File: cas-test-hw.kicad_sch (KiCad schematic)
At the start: 3 parts

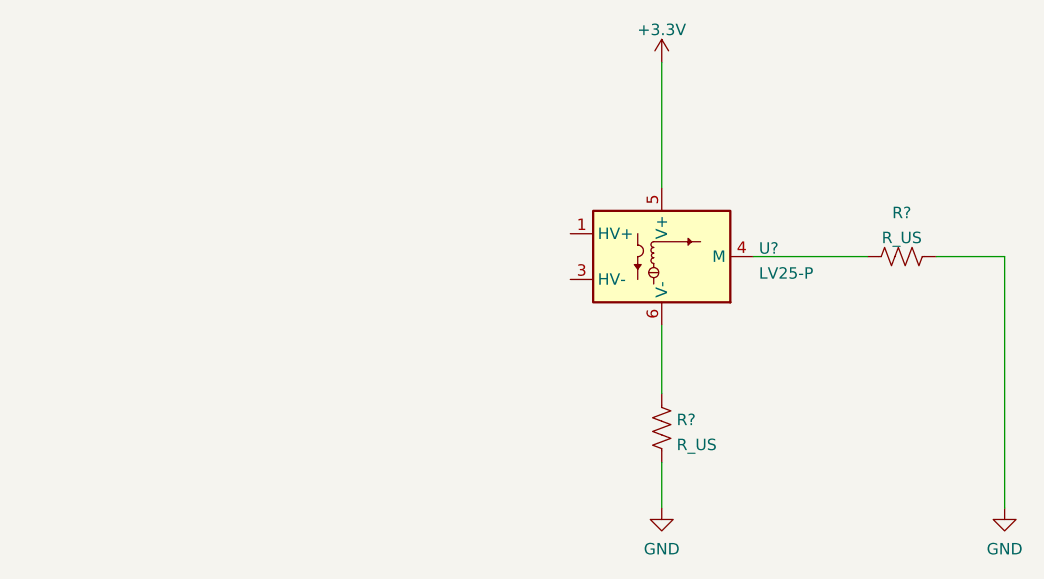
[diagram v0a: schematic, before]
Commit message: added mosfet
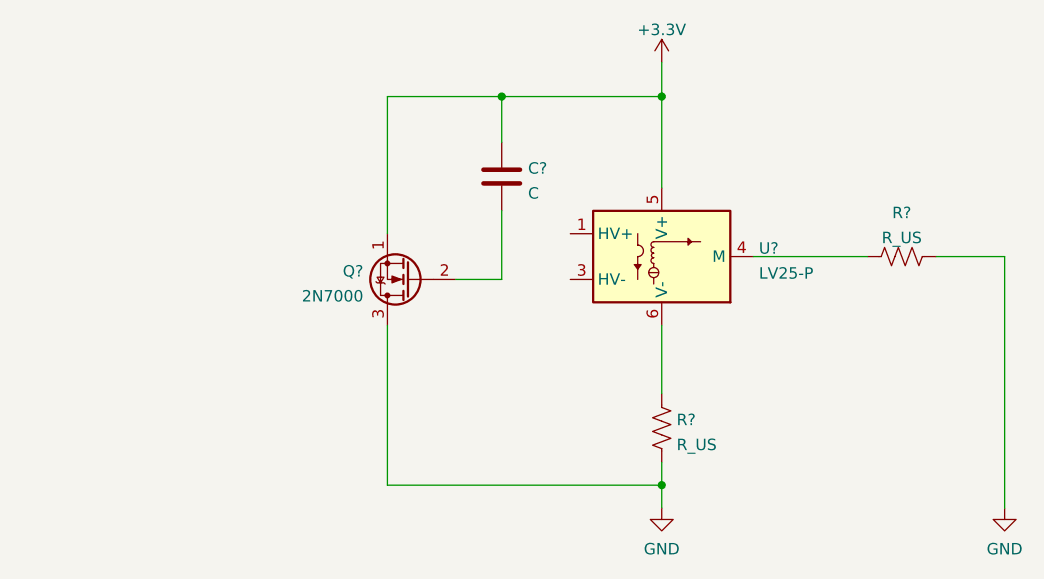
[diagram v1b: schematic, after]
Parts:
- added C?: C, symbol Device:C
- added Q?: 2N7000, Package_TO_SOT_THT:TO-92_Inline, symbol Transistor_FET:2N7000
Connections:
- net +3V3: now also C?.1, Q?.1 (S)
- net GND: now also Q?.3 (D)
- new net: C?.2, Q?.2 (G)
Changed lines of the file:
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@@
 (kicad_sch (version 20210621) (generator eeschema)
   (paper "A4")
-  (wire (pts (xy 123.19 78.74) (xy 123.19 92.71))
+  (junction (at 105.41 82.55) (diameter 0) (color 0 0 0 0))
+  (junction (at 123.19 82.55) (diameter 0) (color 0 0 0 0))
+  (junction (at 123.19 125.73) (diameter 0) (color 0 0 0 0))
+  (wire (pts (xy 92.71 82.55) (xy 105.41 82.55))
+    (stroke (width 0) (type default) (color 0 0 0 0))
+  )
+  (wire (pts (xy 92.71 97.79) (xy 92.71 82.55))
+    (stroke (width 0) (type default) (color 0 0 0 0))
+  )
+  (wire (pts (xy 92.71 107.95) (xy 92.71 125.73))
+    (stroke (width 0) (type default) (color 0 0 0 0))
+  )
+  (wire (pts (xy 92.71 125.73) (xy 123.19 125.73))
+    (stroke (width 0) (type default) (color 0 0 0 0))
+  )
+  (wire (pts (xy 100.33 102.87) (xy 105.41 102.87))
+    (stroke (width 0) (type default) (color 0 0 0 0))
+  )
+  (wire (pts (xy 105.41 82.55) (xy 105.41 87.63))
+    (stroke (width 0) (type default) (color 0 0 0 0))
+  )
+  (wire (pts (xy 105.41 82.55) (xy 123.19 82.55))
+    (stroke (width 0) (type default) (color 0 0 0 0))
+  )
+  (wire (pts (xy 105.41 95.25) (xy 105.41 102.87))
+    (stroke (width 0) (type default) (color 0 0 0 0))
+  )
+  (wire (pts (xy 123.19 78.74) (xy 123.19 82.55))
+    (stroke (width 0) (type default) (color 0 0 0 0))
+  )
+  (wire (pts (xy 123.19 82.55) (xy 123.19 92.71))
     (stroke (width 0) (type default) (color 0 0 0 0))
   )
@@
     (stroke (width 0) (type default) (color 0 0 0 0))
   )
-  (wire (pts (xy 123.19 123.19) (xy 123.19 128.27))
+  (wire (pts (xy 123.19 123.19) (xy 123.19 125.73))
+    (stroke (width 0) (type default) (color 0 0 0 0))
+  )
+  (wire (pts (xy 123.19 125.73) (xy 123.19 128.27))
     (stroke (width 0) (type default) (color 0 0 0 0))
   )
@@
     (pin "1")
     (pin "2")
+  )
+  (symbol (lib_id "Device:C") (at 105.41 91.44 0) (unit 1)
+    (in_bom yes) (on_board yes) (fields_autoplaced)
+    (property "Reference" "C?" (id 0) (at 108.331 90.5315 0)
+      (effects (font (size 1.27 1.27)) (justify left))
+    )
+    (property "Value" "C" (id 1) (at 108.331 93.3066 0)
+      (effects (font (size 1.27 1.27)) (justify left))
+    )
+    (property "Footprint" "" (id 2) (at 106.3752 95.25 0)
+      (effects (font (size 1.27 1.27)) hide)
+    )
+    (property "Datasheet" "~" (id 3) (at 105.41 91.44 0)
+      (effects (font (size 1.27 1.27)) hide)
+    )
+    (pin "1")
+    (pin "2")
+  )
+  (symbol (lib_id "Transistor_FET:2N7000") (at 95.25 102.87 180) (unit 1)
+    (in_bom yes) (on_board yes) (fields_autoplaced)
+    (property "Reference" "Q?" (id 0) (at 90.043 101.9615 0)
+      (effects (font (size 1.27 1.27)) (justify left))
+    )
+    (property "Value" "2N7000" (id 1) (at 90.043 104.7366 0)
+      (effects (font (size 1.27 1.27)) (justify left))
+    )
+    (property "Footprint" "Package_TO_SOT_THT:TO-92_Inline" (id 2) (at 90.17 100.965 0)
+      (effects (font (size 1.27 1.27) italic) (justify left) hide)
+    )
+    (property "Datasheet" "https://www.onsemi.com/pub/Collateral/NDS7002A-D.PDF" (id 3) (at 95.25 102.87 0)
+      (effects (font (size 1.27 1.27)) (justify left) hide)
+    )
+    (pin "1")
+    (pin "2")
+    (pin "3")
   )
   (symbol (lib_id "Sensor_Voltage:LV25-P") (at 123.19 100.33 0) (unit 1)
@@
       (reference "#PWR?") (unit 1) (value "GND") (footprint "")
     )
+    (path "/f3cbb385-5d5b-4802-a5c7-511f3f3faef6"
+      (reference "C?") (unit 1) (value "C") (footprint "")
+    )
+    (path "/31f72fb0-d275-4aa4-b7ef-002a0a293743"
+      (reference "Q?") (unit 1) (value "2N7000") (footprint "Package_TO_SOT_THT:TO-92_Inline")
+    )
     (path "/25fb7c40-108e-4c3b-a612-05be54d655cb"

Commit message: added sam's changes
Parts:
- added Q?: 2N2219, Package_TO_SOT_THT:TO-39-3, symbol Transistor_BJT:2N2219
- added R?: R_Small_US, symbol Device:R_Small_US
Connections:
- net GND: now also R?.2
- net at U?.1 (HV+): now also Q?.2 (B)
- new net: Q?.3 (C), R?.1
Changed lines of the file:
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@@
 (kicad_sch (version 20210621) (generator eeschema)
   (paper "A4")
+  (junction (at 92.71 124.46) (diameter 0) (color 0 0 0 0))
   (junction (at 105.41 82.55) (diameter 0) (color 0 0 0 0))
   (junction (at 123.19 82.55) (diameter 0) (color 0 0 0 0))
   (junction (at 123.19 125.73) (diameter 0) (color 0 0 0 0))
+  (wire (pts (xy 62.23 101.6) (xy 62.23 114.3))
+    (stroke (width 0) (type default) (color 0 0 0 0))
+  )
+  (wire (pts (xy 62.23 119.38) (xy 62.23 124.46))
+    (stroke (width 0) (type default) (color 0 0 0 0))
+  )
+  (wire (pts (xy 62.23 124.46) (xy 92.71 124.46))
+    (stroke (width 0) (type default) (color 0 0 0 0))
+  )
+  (wire (pts (xy 69.85 96.52) (xy 113.03 96.52))
+    (stroke (width 0) (type default) (color 0 0 0 0))
+  )
   (wire (pts (xy 92.71 82.55) (xy 105.41 82.55))
     (stroke (width 0) (type default) (color 0 0 0 0))
@@
     (stroke (width 0) (type default) (color 0 0 0 0))
   )
-  (wire (pts (xy 92.71 107.95) (xy 92.71 125.73))
+  (wire (pts (xy 92.71 107.95) (xy 92.71 124.46))
+    (stroke (width 0) (type default) (color 0 0 0 0))
+  )
+  (wire (pts (xy 92.71 124.46) (xy 92.71 125.73))
     (stroke (width 0) (type default) (color 0 0 0 0))
   )
@@
   )
   (wire (pts (xy 105.41 95.25) (xy 105.41 102.87))
+    (stroke (width 0) (type default) (color 0 0 0 0))
+  )
+  (wire (pts (xy 113.03 96.52) (xy 113.03 97.79))
     (stroke (width 0) (type default) (color 0 0 0 0))
   )
@@
     )
     (pin "1")
+  )
+  (symbol (lib_id "Device:R_Small_US") (at 62.23 116.84 0) (unit 1)
+    (in_bom yes) (on_board yes) (fields_autoplaced)
+    (property "Reference" "R?" (id 0) (at 63.881 115.9315 0)
+      (effects (font (size 1.27 1.27)) (justify left))
+    )
+    (property "Value" "R_Small_US" (id 1) (at 63.881 118.7066 0)
+      (effects (font (size 1.27 1.27)) (justify left))
+    )
+    (property "Footprint" "" (id 2) (at 62.23 116.84 0)
+      (effects (font (size 1.27 1.27)) hide)
+    )
+    (property "Datasheet" "~" (id 3) (at 62.23 116.84 0)
+      (effects (font (size 1.27 1.27)) hide)
+    )
+    (pin "1")
+    (pin "2")
   )
   (symbol (lib_id "Device:R_US") (at 123.19 119.38 0) (unit 1)
@@
     (pin "1")
     (pin "2")
+  )
+  (symbol (lib_id "Transistor_BJT:2N2219") (at 64.77 96.52 180) (unit 1)
+    (in_bom yes) (on_board yes) (fields_autoplaced)
+    (property "Reference" "Q?" (id 0) (at 59.9186 95.6115 0)
+      (effects (font (size 1.27 1.27)) (justify left))
+    )
+    (property "Value" "2N2219" (id 1) (at 59.9186 98.3866 0)
+      (effects (font (size 1.27 1.27)) (justify left))
+    )
+    (property "Footprint" "Package_TO_SOT_THT:TO-39-3" (id 2) (at 59.69 94.615 0)
+      (effects (font (size 1.27 1.27) italic) (justify left) hide)
+    )
+    (property "Datasheet" "http://www.onsemi.com/pub_link/Collateral/2N2219-D.PDF" (id 3) (at 64.77 96.52 0)
+      (effects (font (size 1.27 1.27)) (justify left) hide)
+    )
+    (pin "1")
+    (pin "2")
+    (pin "3")
   )
   (symbol (lib_id "Transistor_FET:2N7000") (at 95.25 102.87 180) (unit 1)
@@
       (reference "Q?") (unit 1) (value "2N7000") (footprint "Package_TO_SOT_THT:TO-92_Inline")
     )
+    (path "/dd3d7d6b-2e35-4397-b03a-a5650a637058"
+      (reference "Q?") (unit 1) (value "2N2219") (footprint "Package_TO_SOT_THT:TO-39-3")
+    )
     (path "/25fb7c40-108e-4c3b-a612-05be54d655cb"
       (reference "R?") (unit 1) (value "R_US") (footprint "")
@@
       (reference "R?") (unit 1) (value "R_US") (footprint "")
     )
+    (path "/df542e4d-5ca4-4e31-b596-0200edf05644"
+      (reference "R?") (unit 1) (value "R_Small_US") (footprint "")
+    )
     (path "/cd7222c6-e829-4e20-bc96-2c7dde7c2e82"
